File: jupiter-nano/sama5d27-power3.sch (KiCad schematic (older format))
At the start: 25 parts, among them U3 MIC5247-2.0YM5-TR

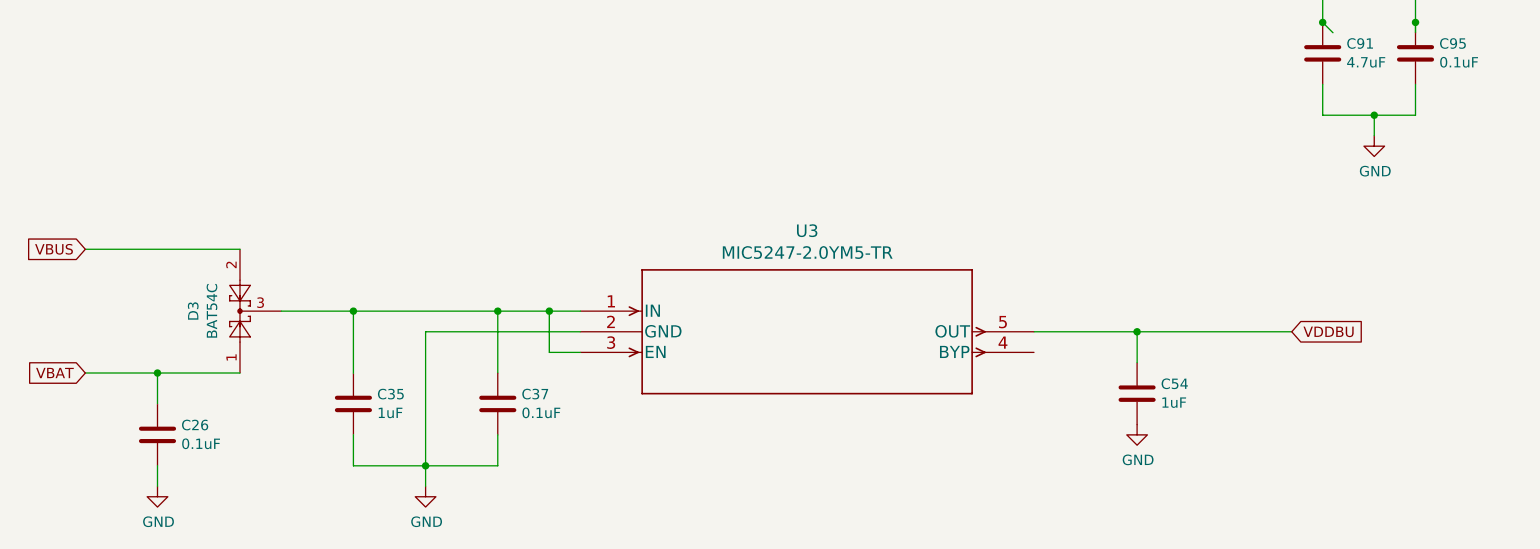
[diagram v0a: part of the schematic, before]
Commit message: added compoent numbers for power
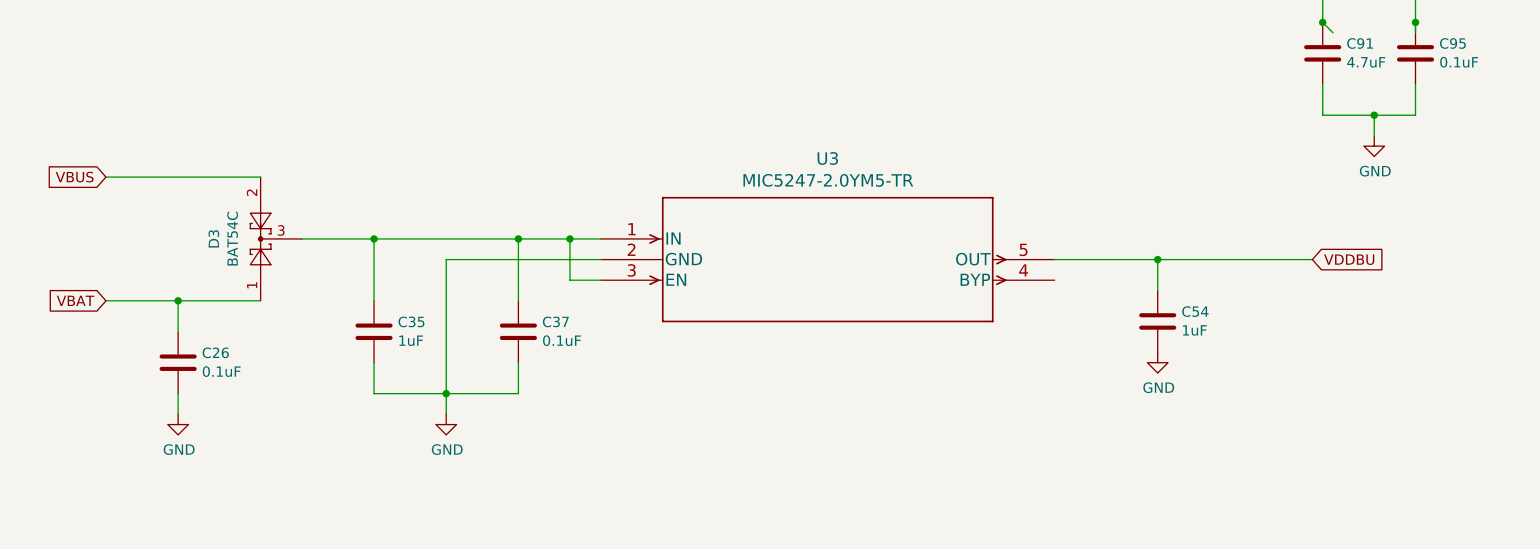
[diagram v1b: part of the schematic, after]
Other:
- moved on the sheet: C26, C35, C37, C54, D3, U3
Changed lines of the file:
@@
 L MIC524720YM5TR:MIC5247-2.0YM5-TR U?
 U 1 1 5FD7EF72
-P 3750 5950
+P 3850 5600
 AR Path="/5F395E67/5FD7EF72" Ref="U?"  Part="1"
 AR Path="/5FD740BF/5FD7EF72" Ref="U3"  Part="1"
-F 0 "U3" H 4850 6338 60  0000 C CNN
-F 1 "MIC5247-2.0YM5-TR" H 4850 6232 60  0000 C CNN
-F 2 "SOT-23-5_M5_MCH" H 4850 6190 60  0001 C CNN
-F 3 "" H 3750 5950 60  0000 C CNN
-	1    3750 5950
+F 0 "U3" H 4950 5988 60  0000 C CNN
+F 1 "MIC5247-2.0YM5-TR" H 4950 5882 60  0000 C CNN
+F 2 "SOT-23-5_M5_MCH" H 4950 5840 60  0001 C CNN
+F 3 "" H 3850 5600 60  0000 C CNN
+	1    3850 5600
 	1    0    0    -1
 $EndComp
@@
 L Diode:BAT54C D?
 U 1 1 5FD7EF78
-P 2100 5950
+P 2200 5600
 AR Path="/5F395E67/5FD7EF78" Ref="D?"  Part="1"
 AR Path="/5FD740BF/5FD7EF78" Ref="D3"  Part="1"
-F 0 "D3" H 2100 6175 50  0000 C CNN
-F 1 "BAT54C" H 2100 6084 50  0000 C CNN
-F 2 "Package_TO_SOT_SMD:SOT-23" H 2175 6075 50  0001 L CNN
-F 3 "http://www.diodes.com/_files/datasheets/ds11005.pdf" H 2020 5950 50  0001 C CNN
-	1    2100 5950
+F 0 "D3" H 2200 5825 50  0000 C CNN
+F 1 "BAT54C" H 2200 5734 50  0000 C CNN
+F 2 "Package_TO_SOT_SMD:SOT-23" H 2275 5725 50  0001 L CNN
+F 3 "http://www.diodes.com/_files/datasheets/ds11005.pdf" H 2120 5600 50  0001 C CNN
+	1    2200 5600
 	0    -1   -1   0
 $EndComp
@@
 L Device:C C35
 U 1 1 5FD81A7E
-P 2650 6400
-F 0 "C35" H 2765 6446 50  0000 L CNN
-F 1 "1uF" H 2765 6355 50  0000 L CNN
-F 2 "Capacitor_SMD:C_0201_0603Metric" H 2688 6250 50  0001 C CNN
-F 3 "~" H 2650 6400 50  0001 C CNN
-	1    2650 6400
+P 2750 6050
+F 0 "C35" H 2865 6096 50  0000 L CNN
+F 1 "1uF" H 2865 6005 50  0000 L CNN
+F 2 "Capacitor_SMD:C_0201_0603Metric" H 2788 5900 50  0001 C CNN
+F 3 "~" H 2750 6050 50  0001 C CNN
+	1    2750 6050
 	1    0    0    -1
 $EndComp
@@
 L Device:C C26
 U 1 1 5FD82B07
-P 1700 6550
-F 0 "C26" H 1815 6596 50  0000 L CNN
-F 1 "0.1uF" H 1815 6505 50  0000 L CNN
-F 2 "Capacitor_SMD:C_0201_0603Metric" H 1738 6400 50  0001 C CNN
-F 3 "~" H 1700 6550 50  0001 C CNN
-	1    1700 6550
+P 1800 6200
+F 0 "C26" H 1915 6246 50  0000 L CNN
+F 1 "0.1uF" H 1915 6155 50  0000 L CNN
+F 2 "Capacitor_SMD:C_0201_0603Metric" H 1838 6050 50  0001 C CNN
+F 3 "~" H 1800 6200 50  0001 C CNN
+	1    1800 6200
 	1    0    0    -1
 $EndComp
@@
 L Device:C C37
 U 1 1 5FD8300B
-P 3350 6400
-F 0 "C37" H 3465 6446 50  0000 L CNN
-F 1 "0.1uF" H 3465 6355 50  0000 L CNN
-F 2 "Capacitor_SMD:C_0201_0603Metric" H 3388 6250 50  0001 C CNN
-F 3 "~" H 3350 6400 50  0001 C CNN
-	1    3350 6400
+P 3450 6050
+F 0 "C37" H 3565 6096 50  0000 L CNN
+F 1 "0.1uF" H 3565 6005 50  0000 L CNN
+F 2 "Capacitor_SMD:C_0201_0603Metric" H 3488 5900 50  0001 C CNN
+F 3 "~" H 3450 6050 50  0001 C CNN
+	1    3450 6050
 	1    0    0    -1
 $EndComp
@@
 L Device:C C54
 U 1 1 5FD85AB1
-P 6450 6350
-F 0 "C54" H 6565 6396 50  0000 L CNN
-F 1 "1uF" H 6565 6305 50  0000 L CNN
-F 2 "Capacitor_SMD:C_0201_0603Metric" H 6488 6200 50  0001 C CNN
-F 3 "~" H 6450 6350 50  0001 C CNN
-	1    6450 6350
+P 6550 6000
+F 0 "C54" H 6665 6046 50  0000 L CNN
+F 1 "1uF" H 6665 5955 50  0000 L CNN
+F 2 "Capacitor_SMD:C_0201_0603Metric" H 6588 5850 50  0001 C CNN
+F 3 "~" H 6550 6000 50  0001 C CNN
+	1    6550 6000
 	1    0    0    -1
 $EndComp
@@
 $EndComp
 Wire Wire Line
-	5950 6050 6450 6050
-Text GLabel 7200 6050 2    50   Input ~ 0
+	6050 5700 6550 5700
+Text GLabel 7300 5700 2    50   Input ~ 0
 VDDBU
 Wire Wire Line
-	6450 6200 6450 6050
-Connection ~ 6450 6050
-Wire Wire Line
-	6450 6050 7200 6050
+	6550 5850 6550 5700
+Connection ~ 6550 5700
+Wire Wire Line
+	6550 5700 7300 5700
 $Comp
 L power:GND #PWR?
 U 1 1 5FD98CB8
-P 6450 6500
-F 0 "#PWR?" H 6450 6250 50  0001 C CNN
-F 1 "GND" H 6455 6327 50  0000 C CNN
-F 2 "" H 6450 6500 50  0001 C CNN
-F 3 "" H 6450 6500 50  0001 C CNN
-	1    6450 6500
-	1    0    0    -1
-$EndComp
-Wire Wire Line
-	2650 6550 2650 6700
-Wire Wire Line
-	2650 6700 3000 6700
-Wire Wire Line
-	3350 6700 3350 6550
-Wire Wire Line
-	3750 6050 3000 6050
-Wire Wire Line
-	3000 6050 3000 6700
-Connection ~ 3000 6700
-Wire Wire Line
-	3000 6700 3350 6700
-Wire Wire Line
-	3000 6700 3000 6800
+P 6550 6150
+F 0 "#PWR?" H 6550 5900 50  0001 C CNN
+F 1 "GND" H 6555 5977 50  0000 C CNN
+F 2 "" H 6550 6150 50  0001 C CNN
+F 3 "" H 6550 6150 50  0001 C CNN
+	1    6550 6150
+	1    0    0    -1
+$EndComp
+Wire Wire Line
+	2750 6200 2750 6350
+Wire Wire Line
+	2750 6350 3100 6350
+Wire Wire Line
+	3450 6350 3450 6200
+Wire Wire Line
+	3850 5700 3100 5700
+Wire Wire Line
+	3100 5700 3100 6350
+Connection ~ 3100 6350
+Wire Wire Line
+	3100 6350 3450 6350
+Wire Wire Line
+	3100 6350 3100 6450
 $Comp
 L power:GND #PWR?
 U 1 1 5FD9D491
-P 3000 6800
-F 0 "#PWR?" H 3000 6550 50  0001 C CNN
-F 1 "GND" H 3005 6627 50  0000 C CNN
-F 2 "" H 3000 6800 50  0001 C CNN
-F 3 "" H 3000 6800 50  0001 C CNN
-	1    3000 6800
-	1    0    0    -1
-$EndComp
-Wire Wire Line
-	3750 5950 3600 5950
-Wire Wire Line
-	3600 5950 3600 6150
-Wire Wire Line
-	3600 6150 3750 6150
-Wire Wire Line
-	3600 5950 3350 5950
-Wire Wire Line
-	3350 5950 3350 6250
-Connection ~ 3600 5950
-Wire Wire Line
-	3350 5950 2650 5950
-Wire Wire Line
-	2650 5950 2650 6250
-Connection ~ 3350 5950
-Wire Wire Line
-	2300 5950 2650 5950
-Connection ~ 2650 5950
-Wire Wire Line
-	2100 5650 1350 5650
-Wire Wire Line
-	2100 6250 1700 6250
-Text GLabel 1350 6250 0    50   Input ~ 0
+P 3100 6450
+F 0 "#PWR?" H 3100 6200 50  0001 C CNN
+F 1 "GND" H 3105 6277 50  0000 C CNN
+F 2 "" H 3100 6450 50  0001 C CNN
+F 3 "" H 3100 6450 50  0001 C CNN
+	1    3100 6450
+	1    0    0    -1
+$EndComp
+Wire Wire Line
+	3850 5600 3700 5600
+Wire Wire Line
+	3700 5600 3700 5800
+Wire Wire Line
+	3700 5800 3850 5800
+Wire Wire Line
+	3700 5600 3450 5600
+Wire Wire Line
+	3450 5600 3450 5900
+Connection ~ 3700 5600
+Wire Wire Line
+	3450 5600 2750 5600
+Wire Wire Line
+	2750 5600 2750 5900
+Connection ~ 3450 5600
+Wire Wire Line
+	2400 5600 2750 5600
+Connection ~ 2750 5600
+Wire Wire Line
+	2200 5300 1450 5300
+Wire Wire Line
+	2200 5900 1800 5900
+Text GLabel 1450 5900 0    50   Input ~ 0
 VBAT
-Text GLabel 1350 5650 0    50   Input ~ 0
+Text GLabel 1450 5300 0    50   Input ~ 0
 VBUS
 Wire Wire Line
-	1700 6400 1700 6250
-Connection ~ 1700 6250
-Wire Wire Line
-	1700 6250 1350 6250
+	1800 6050 1800 5900
+Connection ~ 1800 5900
+Wire Wire Line
+	1800 5900 1450 5900
 $Comp
 L power:GND #PWR?
 U 1 1 5FDA258D
-P 1700 6800
-F 0 "#PWR?" H 1700 6550 50  0001 C CNN
-F 1 "GND" H 1705 6627 50  0000 C CNN
-F 2 "" H 1700 6800 50  0001 C CNN
-F 3 "" H 1700 6800 50  0001 C CNN
-	1    1700 6800
-	1    0    0    -1
-$EndComp
-Wire Wire Line
-	1700 6700 1700 6800
+P 1800 6450
+F 0 "#PWR?" H 1800 6200 50  0001 C CNN
+F 1 "GND" H 1805 6277 50  0000 C CNN
+F 2 "" H 1800 6450 50  0001 C CNN
+F 3 "" H 1800 6450 50  0001 C CNN
+	1    1800 6450
+	1    0    0    -1
+$EndComp
+Wire Wire Line
+	1800 6350 1800 6450
 Text GLabel 8300 1000 2    50   Input ~ 0
 VDDIOP2
